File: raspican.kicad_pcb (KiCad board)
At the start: 2 copper layers, 85 x 56 mm, 26 parts, among them J1 CANBUS, J2 TTL_SERIAL, J3 TERMINATE, P1 CONN_13X2, SW1 BUTTON_FRAME, SW2 BUTTON_FRAME, U1 MCP2551-I/P, U4 MCP2515, Y1 16MHz

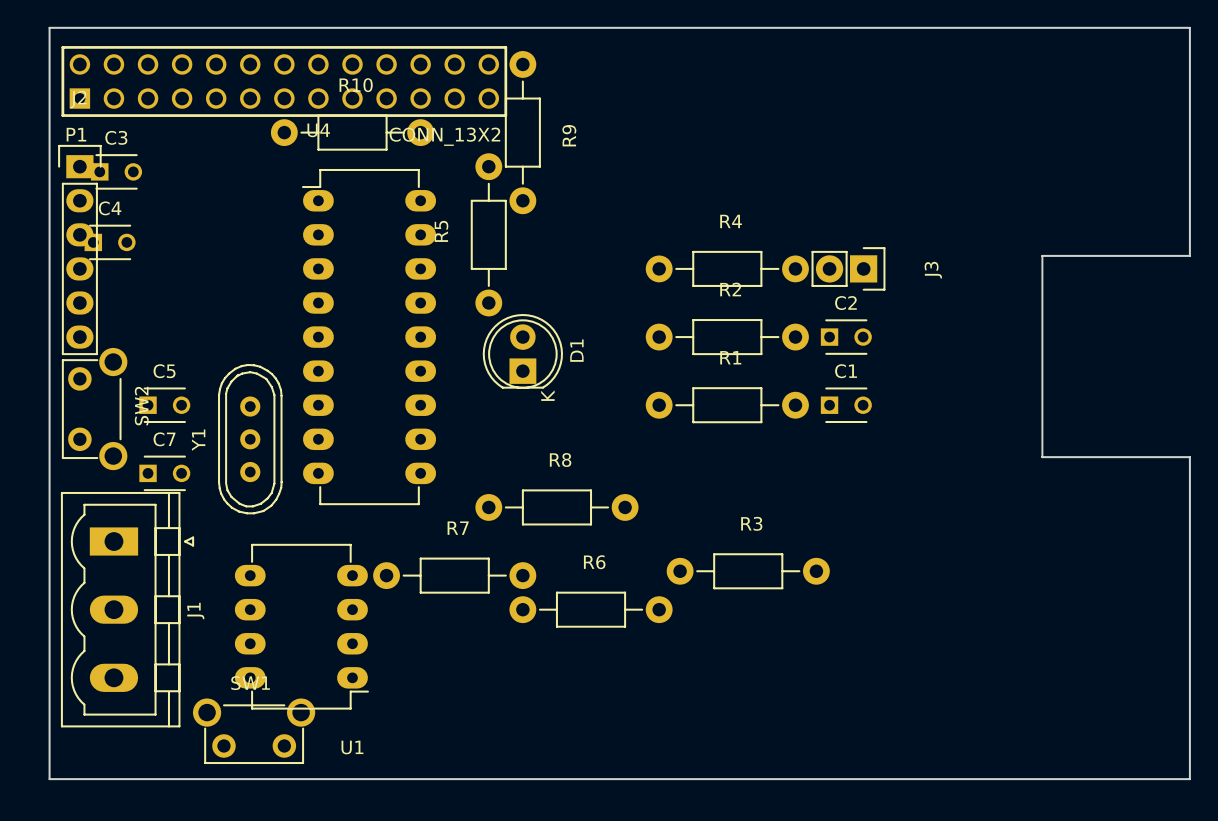
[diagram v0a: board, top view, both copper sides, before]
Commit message: move footprints around, aligned with grid
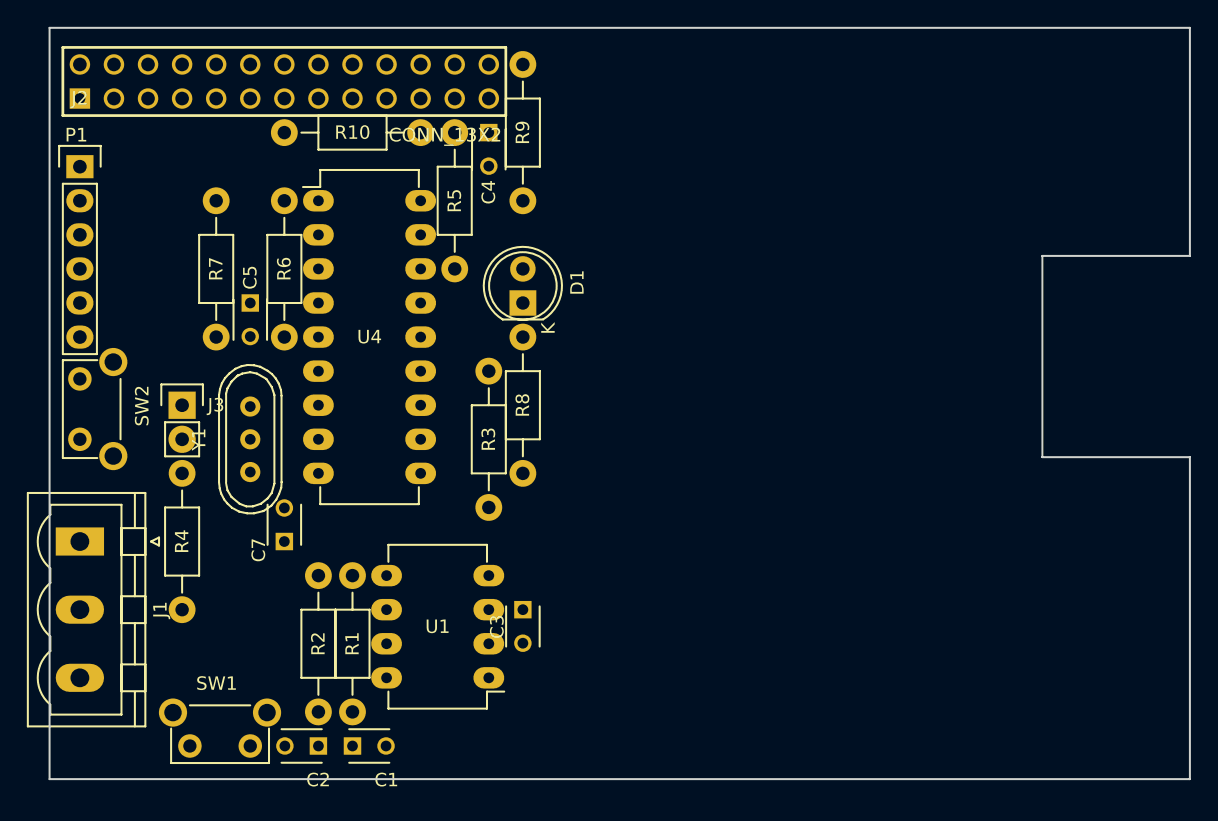
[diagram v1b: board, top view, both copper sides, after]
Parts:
- moved J3 51.8 mm to (153.4, 153.1), turned to 0 degrees
- moved C2 48.8 mm to (163.5, 178.5), turned to 180 degrees
- moved C3 45.4 mm to (178.8, 168.4), turned to 270 degrees
- moved R4 43.7 mm to (153.4, 168.4), turned to 90 degrees
- moved C1 43.7 mm to (166.1, 178.5)
- moved R6 35.3 mm to (161.0, 137.9), turned to 270 degrees
- moved R2 31.0 mm to (163.5, 165.8), turned to 270 degrees
- moved C4 30.6 mm to (176.2, 132.8), turned to 270 degrees
- moved R1 26.2 mm to (166.1, 165.8), turned to 270 degrees
- moved R7 21.8 mm to (155.9, 148.1), turned to 90 degrees
- moved R3 20.6 mm to (176.2, 150.6), turned to 270 degrees
- moved R5 13.0 mm to (173.7, 132.8), turned to 270 degrees
- moved C7 11.4 mm to (161.0, 163.3), turned to 90 degrees
- moved C5 10.8 mm to (158.5, 145.5), turned to 270 degrees
- moved U1 10.2 mm to (176.2, 173.4)
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
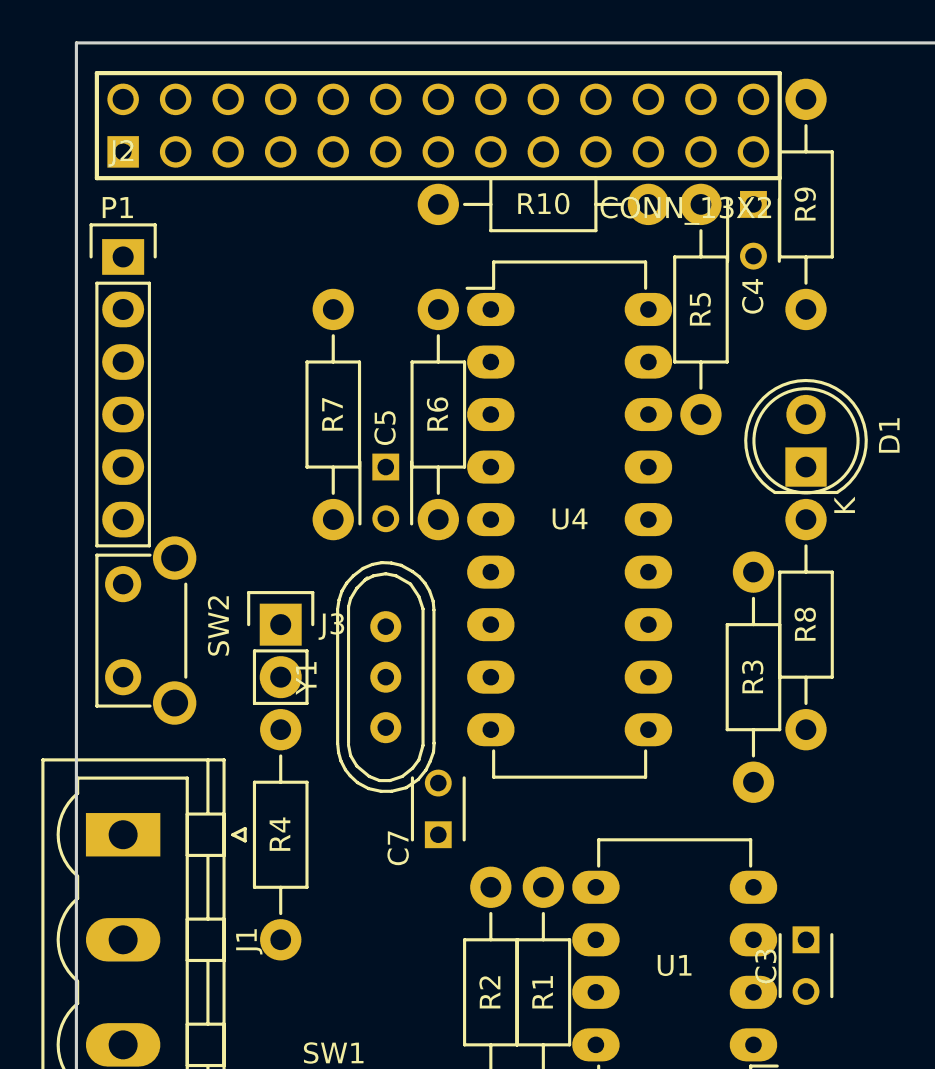
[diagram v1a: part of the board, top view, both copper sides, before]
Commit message: add custom trace widths and start running traces
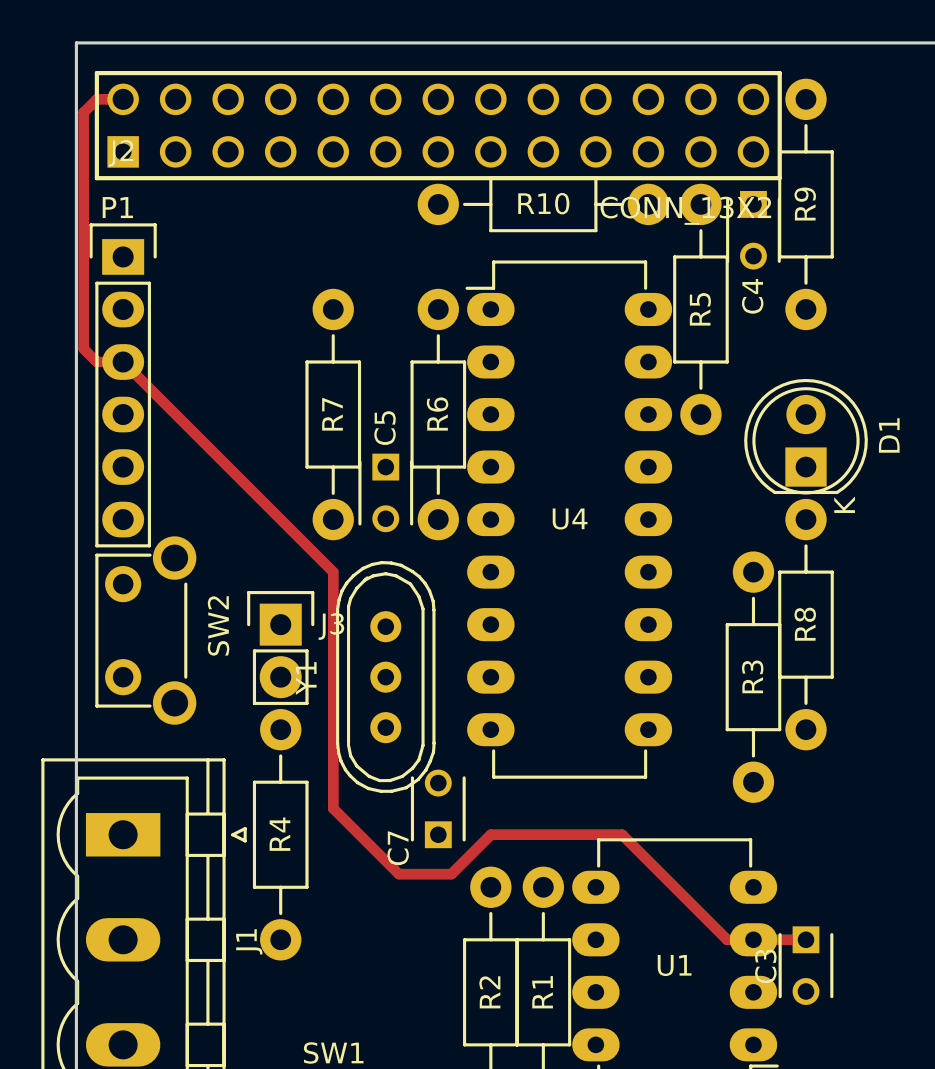
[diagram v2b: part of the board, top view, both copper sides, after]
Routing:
- net +5V: track 0.00 -> 68.6 mm
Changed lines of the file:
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@@
   (general
     (links 57)
-    (no_connects 57)
+    (no_connects 54)
     (area 127.666667 112.000001 242.904763 191.6478)
     (thickness 1.6)
     (drawings 41)
-    (tracks 0)
+    (tracks 14)
     (zones 0)
     (modules 26)
@@
   )
   (setup
-    (last_trace_width 0.2)
+    (last_trace_width 0.508)
+    (user_trace_width 0.254)
+    (user_trace_width 0.508)
+    (user_trace_width 0.762)
+    (user_trace_width 1.016)
+    (user_trace_width 1.27)
     (trace_clearance 0.2)
     (zone_clearance 0.508)
@@
     (uvia_drill 0.1)
     (uvias_allowed no)
-    (uvia_min_size 0.5)
-    (uvia_min_drill 0.1)
+    (uvia_min_size 0)
+    (uvia_min_drill 0)
     (pcb_text_width 0.3)
     (pcb_text_size 1 1)
@@
   (gr_line (start 143.5 181) (end 228.5 181) (angle 90) (layer Edge.Cuts) (width 0.15))
   (gr_line (start 143.5 125) (end 143.5 181) (angle 90) (layer Edge.Cuts) (width 0.15))
+  (segment (start 176.24 168.37) (end 178.78 168.37) (width 0.508) (layer F.Cu) (net 2) (status C00000))
+  (segment (start 145.76 140.43) (end 155.92 150.59) (width 0.508) (layer F.Cu) (net 2) (status 400000))
+  (segment (start 174.97 168.37) (end 176.24 168.37) (width 0.508) (layer F.Cu) (net 2) (status 800000))
+  (segment (start 169.89 163.29) (end 174.97 168.37) (width 0.508) (layer F.Cu) (net 2))
+  (segment (start 163.54 163.29) (end 169.89 163.29) (width 0.508) (layer F.Cu) (net 2))
+  (segment (start 161.635 165.195) (end 163.54 163.29) (width 0.508) (layer F.Cu) (net 2))
+  (segment (start 159.095 165.195) (end 161.635 165.195) (width 0.508) (layer F.Cu) (net 2))
+  (segment (start 155.92 162.02) (end 159.095 165.195) (width 0.508) (layer F.Cu) (net 2))
+  (segment (start 155.92 150.59) (end 155.92 162.02) (width 0.508) (layer F.Cu) (net 2))
+  (segment (start 145.76 140.43) (end 144.49 140.43) (width 0.508) (layer F.Cu) (net 2) (status 400000))
+  (segment (start 144.49 127.73) (end 145.76 127.73) (width 0.508) (layer F.Cu) (net 2) (status 800000))
+  (segment (start 143.855 128.365) (end 144.49 127.73) (width 0.508) (layer F.Cu) (net 2))
+  (segment (start 143.855 139.795) (end 143.855 128.365) (width 0.508) (layer F.Cu) (net 2))
+  (segment (start 144.49 140.43) (end 143.855 139.795) (width 0.508) (layer F.Cu) (net 2))
 )

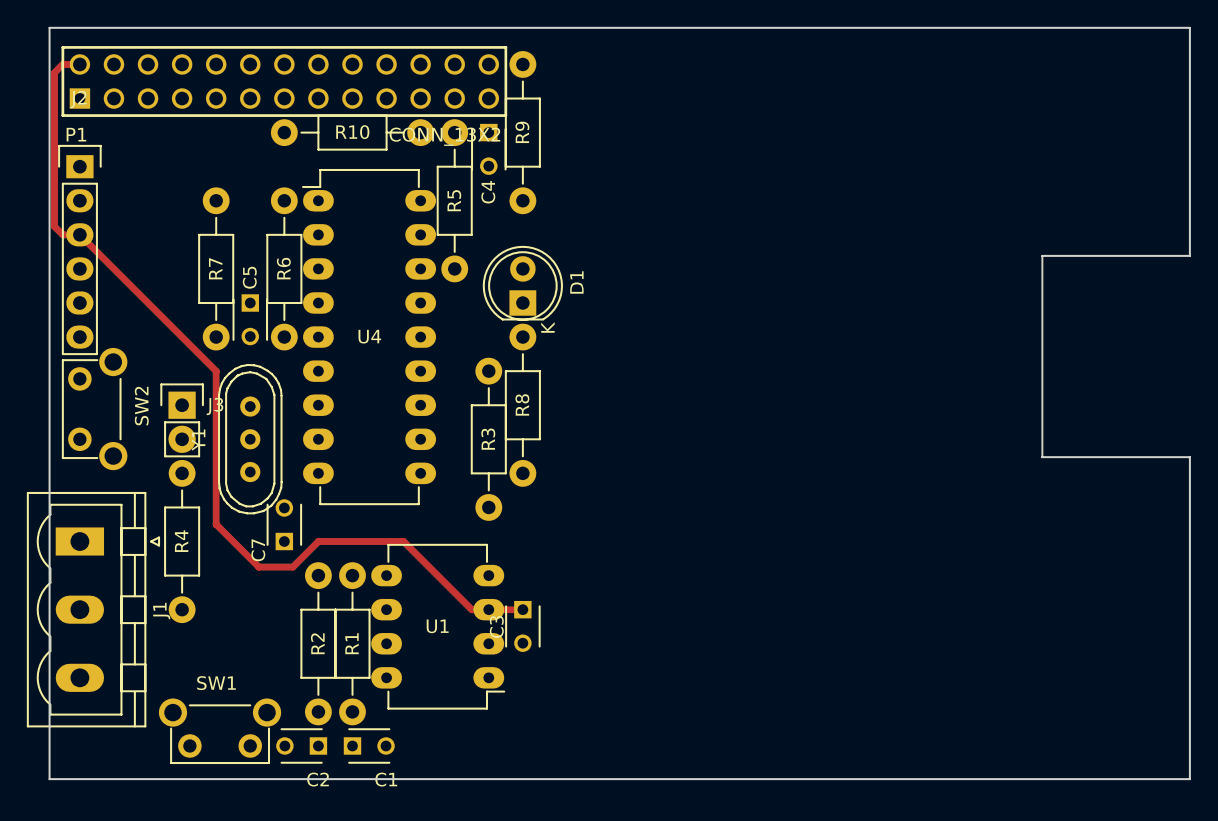
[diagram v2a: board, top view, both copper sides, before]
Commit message: ok i ran all the traces except ground. and no more buttons.
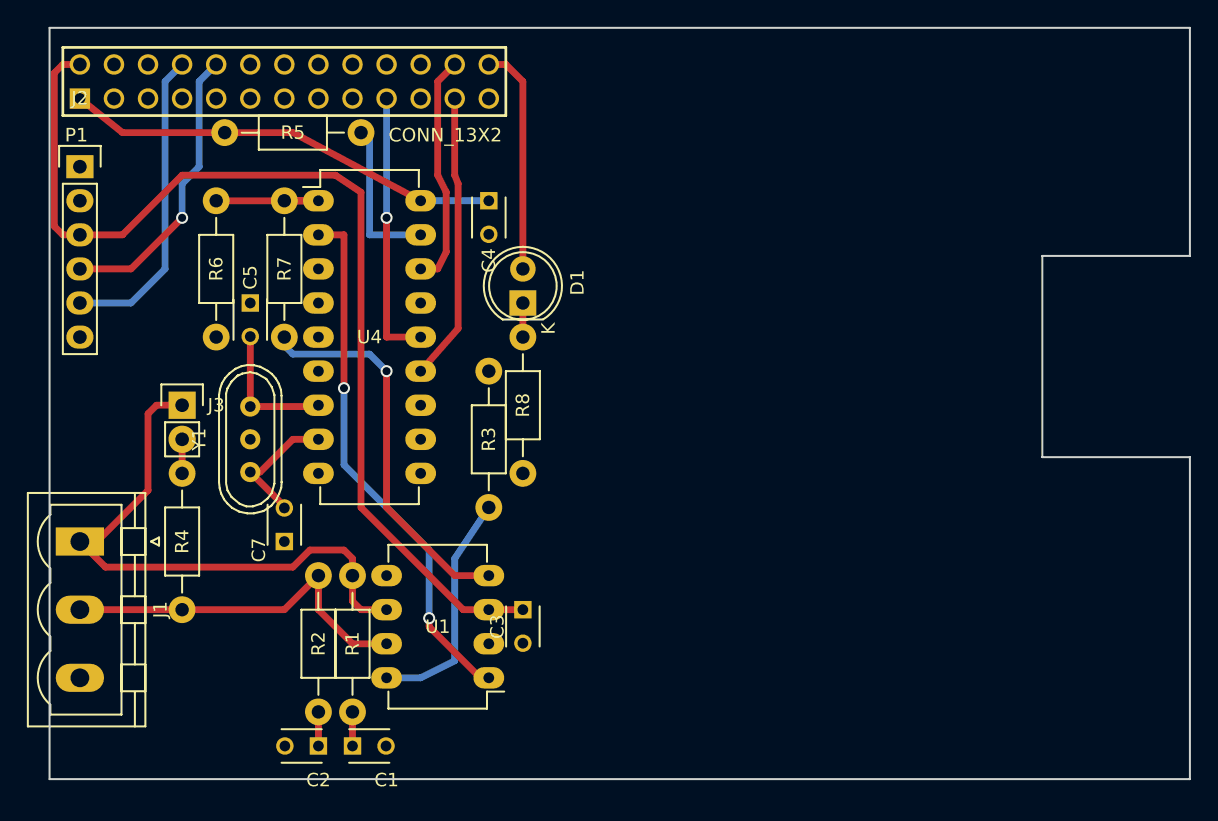
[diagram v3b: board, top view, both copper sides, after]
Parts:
- removed R10, R9: 1KΩ, Resistors_ThroughHole:Resistor_Horizontal_RM10mm
- removed SW1, SW2: BUTTON_FRAME, Buttons_Switches_ThroughHole:SW_Tactile_SPST_Angled
- moved R5 17.1 mm to (156.6, 132.8), turned to 0 degrees
- moved R6 5.08 mm to (155.9, 137.9)
- moved R7 5.08 mm to (161.0, 148.1)
- moved C4 5.08 mm to (176.2, 137.9)
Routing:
- net /CANL: track 0.00 -> 43.1 mm
- net Net-(U1-Pad1): track 0.00 -> 39.8 mm, vias 0 -> 2
- net +3.3V: track 0.00 -> 32.0 mm
- net Net-(R7-Pad1): track 0.00 -> 28.9 mm, vias 0 -> 1
- net /CANH: track 0.00 -> 27.5 mm
- net /TXD: track 0.00 -> 23.2 mm
- net /RXD: track 0.00 -> 21.7 mm, vias 0 -> 1
- net /GPIO11(SCLK): track 0.00 -> 21.4 mm
- net /GPIO10(MOSI): track 0.00 -> 20.3 mm, vias 0 -> 1
- net Net-(R3-Pad2): track 0.00 -> 17.6 mm
- net /GPIO8(CE0): track 0.00 -> 17.3 mm
- net /GPIO7(CE1): track 0.00 -> 17.0 mm
- net Net-(R6-Pad1): track 0.00 -> 12.7 mm
- net Net-(R5-Pad2): track 0.00 -> 11.7 mm
- net Net-(C5-Pad2): track 0.00 -> 10.3 mm
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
